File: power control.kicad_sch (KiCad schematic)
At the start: 10 parts, among them J20 Conn_01x05_Pin, Q1 N MOSFET, Q2 Q_NPN_BCE

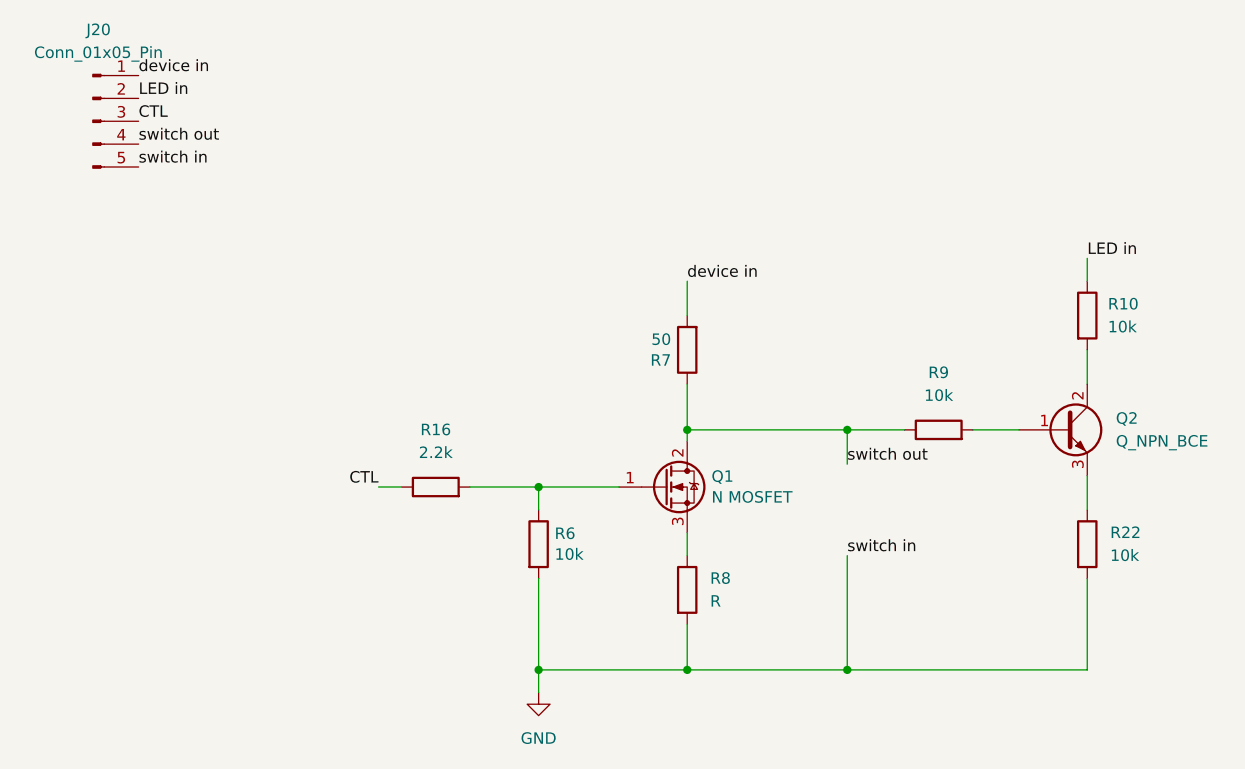
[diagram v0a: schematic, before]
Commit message: Update connectors to be smaller
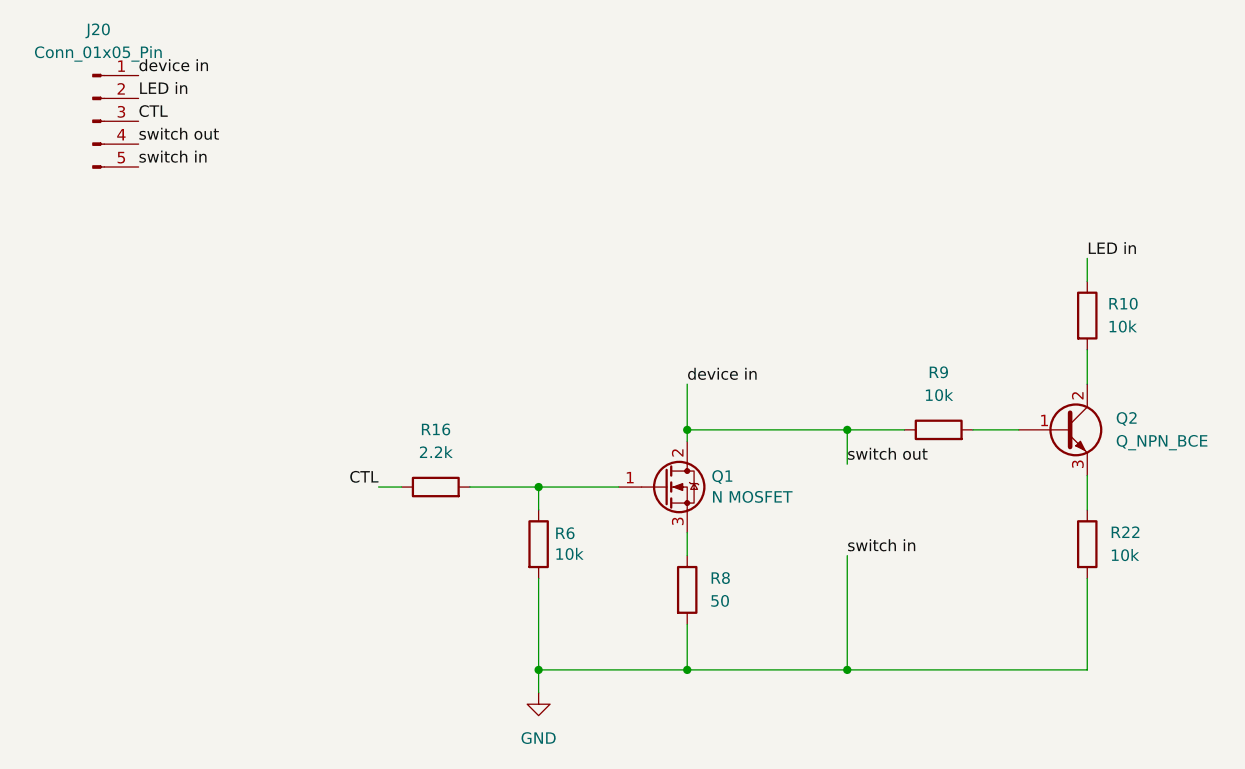
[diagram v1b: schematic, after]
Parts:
- removed R7: 50, Resistor_THT:R_Axial_DIN0207_L6.3mm_D2.5mm_P7.62mm_Horizontal, symbol Device:R
- R8: value R -> 50
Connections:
- net switch out is gone; now on net device in: J20.4 (Pin_4), Q1.2 (D), R9.1
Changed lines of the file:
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@@
-	(wire
-		(pts
-			(xy 143.51 68.58) (xy 143.51 72.39)
-		)
-		(stroke
-			(width 0)
-			(type default)
-		)
-	)
 	(wire
 		(pts
@@
 	)
 	(label "device in"
-		(at 143.51 68.58 0)
+		(at 143.51 80.01 0)
 		(fields_autoplaced yes)
 		(effects
@@
 	(symbol
 		(lib_id "Device:R")
-		(at 143.51 76.2 180)
-		(unit 1)
-		(exclude_from_sim no)
-		(in_bom yes)
-		(on_board yes)
-		(dnp no)
-		(property "Reference" "R7"
-			(at 141.732 77.3684 0)
-			(effects
-				(font
-					(size 1.27 1.27)
-				)
-				(justify left)
-			)
-		)
-		(property "Value" "50"
-			(at 141.732 75.057 0)
-			(effects
-				(font
-					(size 1.27 1.27)
-				)
-				(justify left)
-			)
-		)
-		(property "Footprint" "Resistor_THT:R_Axial_DIN0207_L6.3mm_D2.5mm_P7.62mm_Horizontal"
-			(at 145.288 76.2 90)
-			(effects
-				(font
-					(size 1.27 1.27)
-				)
-				(hide yes)
-			)
-		)
-		(property "Datasheet" ""
-			(at 143.51 76.2 0)
-			(effects
-				(font
-					(size 1.27 1.27)
-				)
-				(hide yes)
-			)
-		)
-		(property "Description" ""
-			(at 143.51 76.2 0)
-			(effects
-				(font
-					(size 1.27 1.27)
-				)
-				(hide yes)
-			)
-		)
-		(property "MPN" "MF-RES-0402-10k"
-			(at 143.51 76.2 0)
-			(effects
-				(font
-					(size 1.27 1.27)
-				)
-				(hide yes)
-			)
-		)
-		(property "POPULATE" "1"
-			(at 143.51 76.2 0)
-			(effects
-				(font
-					(size 1.27 1.27)
-				)
-				(hide yes)
-			)
-		)
-		(pin "1"
-		)
-		(pin "2"
-		)
-		(instances
-			(project "behavior_panel"
-				(path "/4f66b314-0f62-4fb6-8c3c-f9c6a75cd3ec/f3836fb3-3a0e-486b-8766-891268655fa3"
-					(reference "R7")
-					(unit 1)
-				)
-				(path "/4f66b314-0f62-4fb6-8c3c-f9c6a75cd3ec/cba2e56b-ee53-4e3f-b78d-df0a8ddc23e4"
-					(reference "R18")
-					(unit 1)
-				)
-				(path "/4f66b314-0f62-4fb6-8c3c-f9c6a75cd3ec/540ef4d7-5fd0-4577-84e4-0498e327b4c8"
-					(reference "R25")
-					(unit 1)
-				)
-				(path "/4f66b314-0f62-4fb6-8c3c-f9c6a75cd3ec/c31bb56b-4d55-49ba-bd60-4a6581744f2a"
-					(reference "R36")
-					(unit 1)
-				)
-			)
-		)
-	)
-	(symbol
-		(lib_id "Device:R")
 		(at 187.96 97.79 0)
 		(unit 1)
@@
 			)
 		)
-		(property "Value" "R"
+		(property "Value" "50"
 			(at 146.05 104.1399 0)
 			(effects

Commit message: Release of V2 of behavior panel
* LED indicators should now be working
* Slightly narrower board
* Added recommended values for footprints
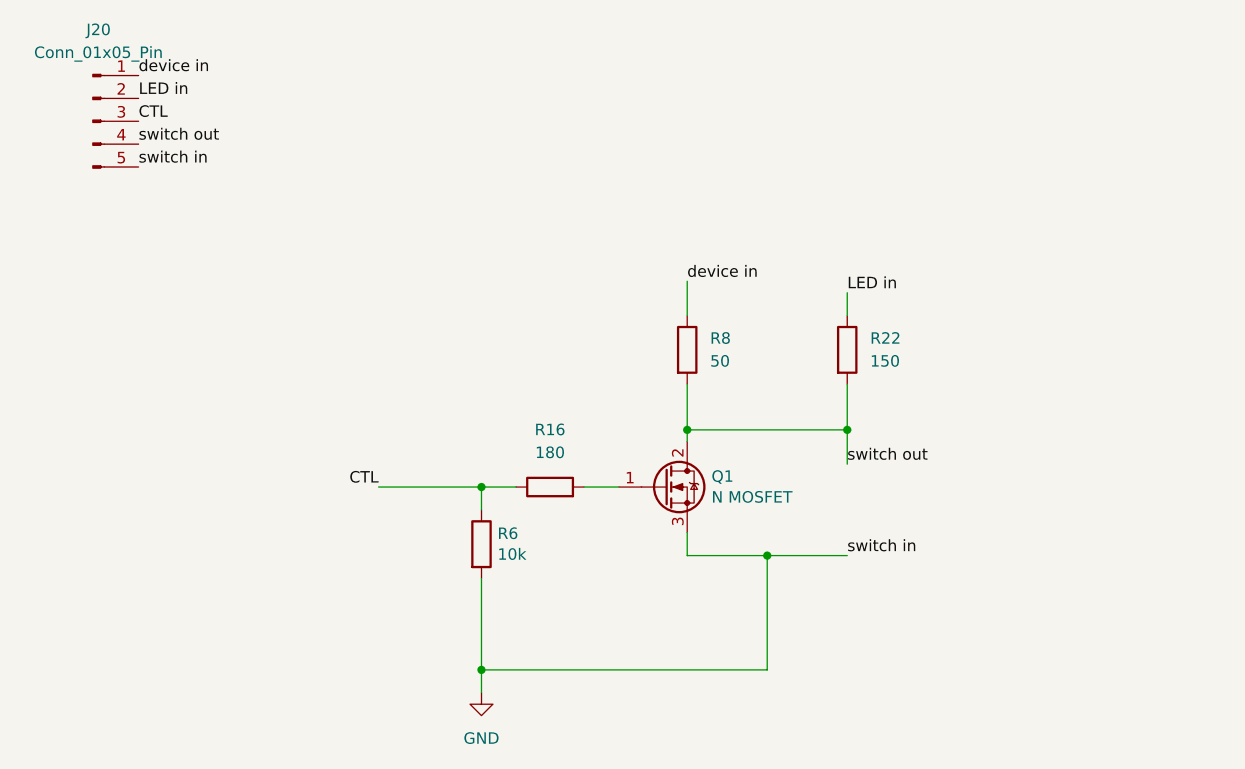
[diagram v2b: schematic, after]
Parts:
- removed Q2: Q_NPN_BCE, Package_TO_SOT_THT:TO-92L_Inline_Wide, symbol Device:Q_NPN_BCE
- removed R10, R9: 10k, Resistor_THT:R_Axial_DIN0207_L6.3mm_D2.5mm_P7.62mm_Horizontal, symbol Device:R
- R16: value 2.2k -> 180
- R22: value 10k -> 150
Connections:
- net CTL: now also R6.1
- net GND: now also Q1.3 (S); no longer R22.2, R8.2
- net LED in: now also R22.1
- net device in: now also R8.1; no longer J20.4 (Pin_4), Q1.2 (D)
- net at Q1.1 (G), R16.2: no longer R6.1
- new net switch out: J20.4 (Pin_4), Q1.2 (D), R22.2, R8.2
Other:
- moved on the sheet: R16, R22, R6, R8

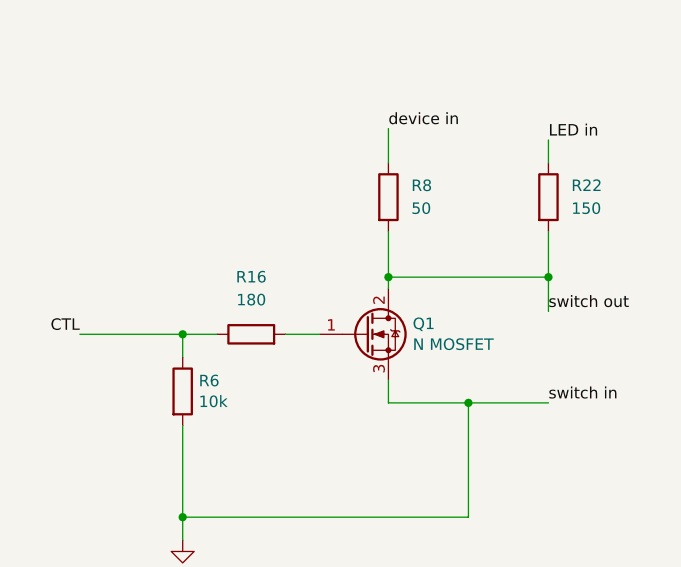
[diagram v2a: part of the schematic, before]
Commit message: Add more ground pins. Fix labels.
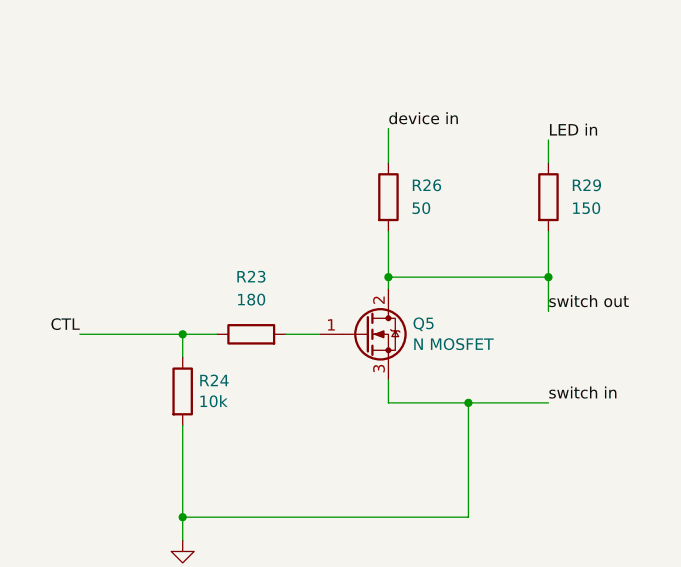
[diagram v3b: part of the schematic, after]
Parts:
- renumbered Q1 to Q5, R16 to R23, R6 to R24, R8 to R26, R22 to R29
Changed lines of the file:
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@@
 	(label "switch in"
 		(at 82.55 55.88 0)
-		(fields_autoplaced yes)
 		(effects
 			(font
@@
 	(label "switch in"
 		(at 161.29 99.06 0)
-		(fields_autoplaced yes)
 		(effects
 			(font
@@
 	(label "device in"
 		(at 82.55 45.72 0)
-		(fields_autoplaced yes)
 		(effects
 			(font
@@
 	(label "CTL"
 		(at 82.55 50.8 0)
-		(fields_autoplaced yes)
 		(effects
 			(font
@@
 	(label "device in"
 		(at 143.51 68.58 0)
-		(fields_autoplaced yes)
 		(effects
 			(font
@@
 	(label "switch out"
 		(at 82.55 53.34 0)
-		(fields_autoplaced yes)
 		(effects
 			(font
@@
 	(label "LED in"
 		(at 161.29 69.85 0)
-		(fields_autoplaced yes)
 		(effects
 			(font
@@
 	(label "LED in"
 		(at 82.55 48.26 0)
-		(fields_autoplaced yes)
 		(effects
 			(font
@@
 	(label "switch out"
 		(at 161.29 88.9 0)
-		(fields_autoplaced yes)
 		(effects
 			(font
@@
 	(label "CTL"
 		(at 109.22 91.44 180)
-		(fields_autoplaced yes)
 		(effects
 			(font
@@
 		(on_board yes)
 		(dnp no)
-		(property "Reference" "R16"
+		(property "Reference" "R23"
 			(at 128.27 85.09 90)
 			(effects
@@
 		(instances
 			(project "behavior_panel"
+				(path "/4f66b314-0f62-4fb6-8c3c-f9c6a75cd3ec/540ef4d7-5fd0-4577-84e4-0498e327b4c8"
+					(reference "R23")
+					(unit 1)
+				)
+				(path "/4f66b314-0f62-4fb6-8c3c-f9c6a75cd3ec/c31bb56b-4d55-49ba-bd60-4a6581744f2a"
+					(reference "R34")
+					(unit 1)
+				)
 				(path "/4f66b314-0f62-4fb6-8c3c-f9c6a75cd3ec/cba2e56b-ee53-4e3f-b78d-df0a8ddc23e4"
 					(reference "R16")
-					(unit 1)
-				)
-				(path "/4f66b314-0f62-4fb6-8c3c-f9c6a75cd3ec/540ef4d7-5fd0-4577-84e4-0498e327b4c8"
-					(reference "R23")
-					(unit 1)
-				)
-				(path "/4f66b314-0f62-4fb6-8c3c-f9c6a75cd3ec/c31bb56b-4d55-49ba-bd60-4a6581744f2a"
-					(reference "R34")
 					(unit 1)
 				)
@@
 		(on_board yes)
 		(dnp no)
-		(property "Reference" "R6"
+		(property "Reference" "R24"
 			(at 122.428 96.6216 0)
 			(effects
@@
 		(instances
 			(project "behavior_panel"
+				(path "/4f66b314-0f62-4fb6-8c3c-f9c6a75cd3ec/540ef4d7-5fd0-4577-84e4-0498e327b4c8"
+					(reference "R24")
+					(unit 1)
+				)
+				(path "/4f66b314-0f62-4fb6-8c3c-f9c6a75cd3ec/c31bb56b-4d55-49ba-bd60-4a6581744f2a"
+					(reference "R35")
+					(unit 1)
+				)
+				(path "/4f66b314-0f62-4fb6-8c3c-f9c6a75cd3ec/cba2e56b-ee53-4e3f-b78d-df0a8ddc23e4"
+					(reference "R17")
+					(unit 1)
+				)
 				(path "/4f66b314-0f62-4fb6-8c3c-f9c6a75cd3ec/f3836fb3-3a0e-486b-8766-891268655fa3"
 					(reference "R6")
-					(unit 1)
-				)
-				(path "/4f66b314-0f62-4fb6-8c3c-f9c6a75cd3ec/cba2e56b-ee53-4e3f-b78d-df0a8ddc23e4"
-					(reference "R17")
-					(unit 1)
-				)
-				(path "/4f66b314-0f62-4fb6-8c3c-f9c6a75cd3ec/540ef4d7-5fd0-4577-84e4-0498e327b4c8"
-					(reference "R24")
-					(unit 1)
-				)
-				(path "/4f66b314-0f62-4fb6-8c3c-f9c6a75cd3ec/c31bb56b-4d55-49ba-bd60-4a6581744f2a"
-					(reference "R35")
 					(unit 1)
 				)
@@
 		(on_board yes)
 		(dnp no)
-		(property "Reference" "Q1"
+		(property "Reference" "Q5"
 			(at 146.2024 90.2716 0)
 			(effects
@@
 		(instances
 			(project "behavior_panel"
+				(path "/4f66b314-0f62-4fb6-8c3c-f9c6a75cd3ec/540ef4d7-5fd0-4577-84e4-0498e327b4c8"
+					(reference "Q5")
+					(unit 1)
+				)
+				(path "/4f66b314-0f62-4fb6-8c3c-f9c6a75cd3ec/c31bb56b-4d55-49ba-bd60-4a6581744f2a"
+					(reference "Q7")
+					(unit 1)
+				)
+				(path "/4f66b314-0f62-4fb6-8c3c-f9c6a75cd3ec/cba2e56b-ee53-4e3f-b78d-df0a8ddc23e4"
+					(reference "Q3")
+					(unit 1)
+				)
 				(path "/4f66b314-0f62-4fb6-8c3c-f9c6a75cd3ec/f3836fb3-3a0e-486b-8766-891268655fa3"
 					(reference "Q1")
-					(unit 1)
-				)
-				(path "/4f66b314-0f62-4fb6-8c3c-f9c6a75cd3ec/cba2e56b-ee53-4e3f-b78d-df0a8ddc23e4"
-					(reference "Q3")
-					(unit 1)
-				)
-				(path "/4f66b314-0f62-4fb6-8c3c-f9c6a75cd3ec/540ef4d7-5fd0-4577-84e4-0498e327b4c8"
-					(reference "Q5")
-					(unit 1)
-				)
-				(path "/4f66b314-0f62-4fb6-8c3c-f9c6a75cd3ec/c31bb56b-4d55-49ba-bd60-4a6581744f2a"
-					(reference "Q7")
 					(unit 1)
 				)
@@
 					(unit 1)
 				)
+				(path "/4f66b314-0f62-4fb6-8c3c-f9c6a75cd3ec/c31bb56b-4d55-49ba-bd60-4a6581744f2a"
+					(reference "J22")
+					(unit 1)
+				)
+				(path "/4f66b314-0f62-4fb6-8c3c-f9c6a75cd3ec/cba2e56b-ee53-4e3f-b78d-df0a8ddc23e4"
+					(reference "J19")
+					(unit 1)
+				)
 				(path "/4f66b314-0f62-4fb6-8c3c-f9c6a75cd3ec/f3836fb3-3a0e-486b-8766-891268655fa3"
 					(reference "J17")
-					(unit 1)
-				)
-				(path "/4f66b314-0f62-4fb6-8c3c-f9c6a75cd3ec/cba2e56b-ee53-4e3f-b78d-df0a8ddc23e4"
-					(reference "J19")
-					(unit 1)
-				)
-				(path "/4f66b314-0f62-4fb6-8c3c-f9c6a75cd3ec/c31bb56b-4d55-49ba-bd60-4a6581744f2a"
-					(reference "J22")
 					(unit 1)
 				)
@@
 		(dnp no)
 		(fields_autoplaced yes)
-		(property "Reference" "#PWR021"
+		(property "Reference" "#PWR024"
 			(at 120.65 120.65 0)
 			(effects
@@
 		(instances
 			(project "behavior_panel"
+				(path "/4f66b314-0f62-4fb6-8c3c-f9c6a75cd3ec/540ef4d7-5fd0-4577-84e4-0498e327b4c8"
+					(reference "#PWR024")
+					(unit 1)
+				)
+				(path "/4f66b314-0f62-4fb6-8c3c-f9c6a75cd3ec/c31bb56b-4d55-49ba-bd60-4a6581744f2a"
+					(reference "#PWR026")
+					(unit 1)
+				)
+				(path "/4f66b314-0f62-4fb6-8c3c-f9c6a75cd3ec/cba2e56b-ee53-4e3f-b78d-df0a8ddc23e4"
+					(reference "#PWR023")
+					(unit 1)
+				)
 				(path "/4f66b314-0f62-4fb6-8c3c-f9c6a75cd3ec/f3836fb3-3a0e-486b-8766-891268655fa3"
 					(reference "#PWR021")
-					(unit 1)
-				)
-				(path "/4f66b314-0f62-4fb6-8c3c-f9c6a75cd3ec/cba2e56b-ee53-4e3f-b78d-df0a8ddc23e4"
-					(reference "#PWR023")
-					(unit 1)
-				)
-				(path "/4f66b314-0f62-4fb6-8c3c-f9c6a75cd3ec/540ef4d7-5fd0-4577-84e4-0498e327b4c8"
-					(reference "#PWR024")
-					(unit 1)
-				)
-				(path "/4f66b314-0f62-4fb6-8c3c-f9c6a75cd3ec/c31bb56b-4d55-49ba-bd60-4a6581744f2a"
-					(reference "#PWR026")
 					(unit 1)
 				)
@@
 		(dnp no)
 		(fields_autoplaced yes)
-		(property "Reference" "R22"
+		(property "Reference" "R29"
 			(at 163.83 74.9299 0)
 			(effects
@@
 		(instances
 			(project "behavior_panel"
+				(path "/4f66b314-0f62-4fb6-8c3c-f9c6a75cd3ec/540ef4d7-5fd0-4577-84e4-0498e327b4c8"
+					(reference "R29")
+					(unit 1)
+				)
+				(path "/4f66b314-0f62-4fb6-8c3c-f9c6a75cd3ec/c31bb56b-4d55-49ba-bd60-4a6581744f2a"
+					(reference "R40")
+					(unit 1)
+				)
 				(path "/4f66b314-0f62-4fb6-8c3c-f9c6a75cd3ec/cba2e56b-ee53-4e3f-b78d-df0a8ddc23e4"
 					(reference "R22")
-					(unit 1)
-				)
-				(path "/4f66b314-0f62-4fb6-8c3c-f9c6a75cd3ec/540ef4d7-5fd0-4577-84e4-0498e327b4c8"
-					(reference "R29")
-					(unit 1)
-				)
-				(path "/4f66b314-0f62-4fb6-8c3c-f9c6a75cd3ec/c31bb56b-4d55-49ba-bd60-4a6581744f2a"
-					(reference "R40")
 					(unit 1)
 				)
@@
 		(on_board yes)
 		(dnp no)
-		(property "Reference" "R8"
+		(property "Reference" "R26"
 			(at 146.05 74.9299 0)
 			(effects
@@
 		(instances
 			(project "behavior_panel"
+				(path "/4f66b314-0f62-4fb6-8c3c-f9c6a75cd3ec/540ef4d7-5fd0-4577-84e4-0498e327b4c8"
+					(reference "R26")
+					(unit 1)
+				)
+				(path "/4f66b314-0f62-4fb6-8c3c-f9c6a75cd3ec/c31bb56b-4d55-49ba-bd60-4a6581744f2a"
+					(reference "R37")
+					(unit 1)
+				)
+				(path "/4f66b314-0f62-4fb6-8c3c-f9c6a75cd3ec/cba2e56b-ee53-4e3f-b78d-df0a8ddc23e4"
+					(reference "R19")
+					(unit 1)
+				)
 				(path "/4f66b314-0f62-4fb6-8c3c-f9c6a75cd3ec/f3836fb3-3a0e-486b-8766-891268655fa3"
 					(reference "R8")
 					(unit 1)
 				)
-				(path "/4f66b314-0f62-4fb6-8c3c-f9c6a75cd3ec/cba2e56b-ee53-4e3f-b78d-df0a8ddc23e4"
-					(reference "R19")
-					(unit 1)
-				)
-				(path "/4f66b314-0f62-4fb6-8c3c-f9c6a75cd3ec/540ef4d7-5fd0-4577-84e4-0498e327b4c8"
-					(reference "R26")
-					(unit 1)
-				)
-				(path "/4f66b314-0f62-4fb6-8c3c-f9c6a75cd3ec/c31bb56b-4d55-49ba-bd60-4a6581744f2a"
-					(reference "R37")
-					(unit 1)
-				)
